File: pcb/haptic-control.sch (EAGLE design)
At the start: 71 parts, among them J1 PAD1X3_5MM-2P, J2 PAD1X3_5MM-2P, M1 SPH0641LM4H-1, U1 CC2642R, U10 FS8205, U2 SST26VF064B, U3 ICM20948, U4 74LVC1G17, U5 MCP1700T-1802TT, U6 PCA9306-DCU, U7 MTCH6301, U8 BQ51050B, U9 FS312F-G, X1 48MHz, X2 32.768kHz

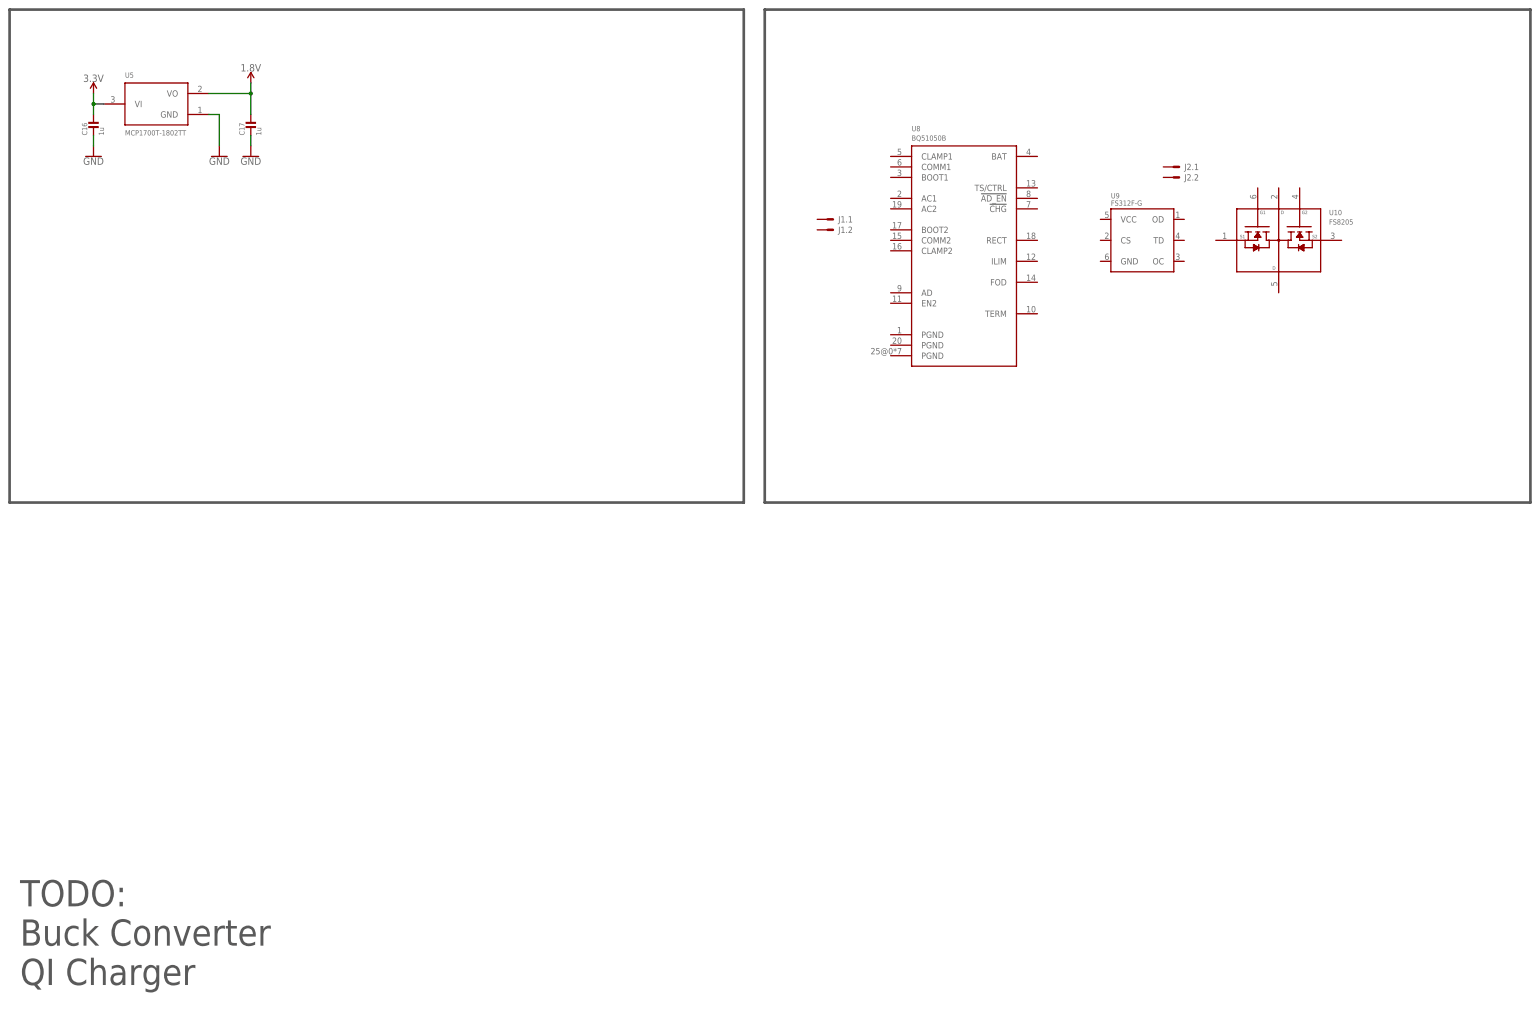
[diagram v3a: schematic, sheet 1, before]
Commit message: added LRA drivers, added FSRs
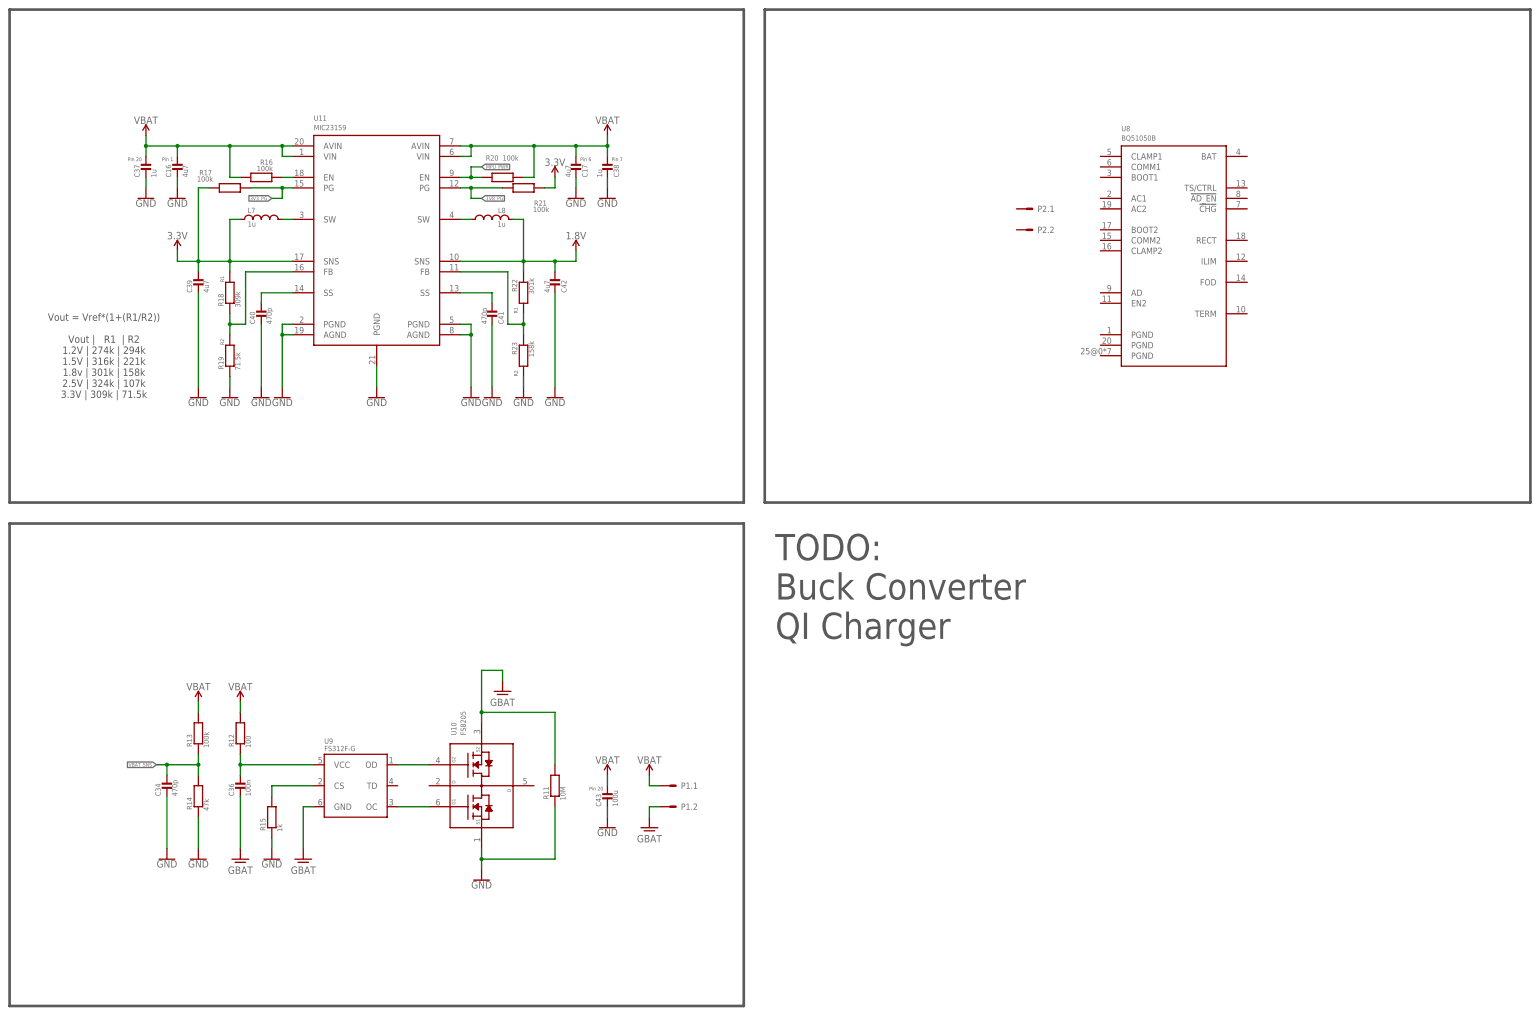
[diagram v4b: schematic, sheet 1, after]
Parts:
- removed J1, J2: PAD1X3_5MM-2P, Connectors > Other:PAD1X3_5MM-2P
- removed TP1, TP2, TP3: TEST_POINT, Utility > Board:TEST_POINT
- added C36, C44, C45: 100n, Passive Components > Capacitors > Multilayer Ceramic Capacitors MLCC:MLCC_0402
- added C37, C38, C46, C47: 1u, Passive Components > Capacitors > Multilayer Ceramic Capacitors MLCC:MLCC0603
- added C39, C42: 4u7, Passive Components > Capacitors > Multilayer Ceramic Capacitors MLCC:MLCC0603
- added C40, C41: 470p, Passive Components > Capacitors > Multilayer Ceramic Capacitors MLCC:MLCC_0402
- added C43: 100u, Passive Components > Capacitors > Multilayer Ceramic Capacitors MLCC:MLCC_1206
- added JP1, JP2: JUMPER-SMT_2_NC_TRACE_SILK, Utility > Board:JUMPER-SMT_2_NC_TRACE_SILK
- added L7, L8: 1u, Passive Components > Inductors, Chokes & Coils:INDUCTOR_NC_0805
- added P1, P2, P3, P4: 2P-PAD_1X3.5, Connectors > Other:2P-PAD_1X3.5
- added R10, R13, R16, R17, R20, R21: 100k, Passive Components > Resistors > Chip Resistors:RESISTOR_0402
- added R11: 10M, Passive Components > Resistors > Chip Resistors:RESISTOR_0402
- added R12: 100, Passive Components > Resistors > Chip Resistors:RESISTOR_0402
- added R14: 47k, Passive Components > Resistors > Chip Resistors:RESISTOR_0402
- added R15: 1k, Passive Components > Resistors > Chip Resistors:RESISTOR_0402
- added R18: 309k, Passive Components > Resistors > Chip Resistors:RESISTOR_0402
- added R19: 71.5k, Passive Components > Resistors > Chip Resistors:RESISTOR_0402
- added R22: 301k, Passive Components > Resistors > Chip Resistors:RESISTOR_0402
- added R23: 158k, Passive Components > Resistors > Chip Resistors:RESISTOR_0402
- added R24, R25, R26, R27: FSR400-SHORT-TAIL, Interlink:FSR400-SHORT-TAIL
- added U11: MIC23159, Microchip:MIC23159
- added U12: DRV2605L, Texas Instruments:DRV2605L
- C16, C17: value 1u -> 4u7
- C27: value 100u -> 22u; device Passive Components > Capacitors > Multilayer Ceramic Capacitors MLCC:MLCC_1206 -> Passive Components > Capacitors > Multilayer Ceramic Capacitors MLCC:MLCC0603
- C33: device Passive Components > Capacitors > Multilayer Ceramic Capacitors MLCC:MLCC_0402 -> Passive Components > Capacitors > Multilayer Ceramic Capacitors MLCC:MLCC_SEL
- C34: value DNP -> 470p
- R8, R9: value 200k -> 4k7
- U5: value MCP1700T-1802TT -> DRV2605L; device Power > LDO Voltage Regulators:MCP1700T-1802TT -> Texas Instruments:DRV2605L
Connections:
- new net 1V8_PG: R21.P$1, U11.PG@1
- new net 3V3_PG: R17.P$1, U11.PG@0
- new net GBAT: C36.P$2, P1.2.S, R11.P$2, U10.S2, U9.GND
- new net LRA_EN: U12.EN, U5.EN
- new net MPU_PWR: R20.P$1, U11.EN@1
- new net N$12: C33.I, L6.P$1
- new net N$13: C32.P$1, C33.O2
- new net N$21: U10.G2, U9.OD
- new net N$22: U10.G1, U9.OC
- new net N$23: C36.P$1, R12.P$1, U9.VCC
- new net N$24: R15.P$2, U9.CS
- new net N$25: R18.P$1, R19.P$2, U11.FB@0
- new net N$26: R16.P$1, U11.EN@0
- new net N$27: P3.1.S, U5.OUT+
- new net N$28: L7.P$2, U11.SW@0
- new net N$29: C40.P$1, U11.SS@0
- new net N$30: L8.P$2, U11.SW@1
- new net N$31: C41.P$1, U11.SS@1
- new net N$32: R22.P$2, R23.P$1, U11.FB@1
- new net N$33: P3.2.S, U5.OUT-
- new net N$34: P4.1.S, U12.OUT+
- new net N$35: P4.2.S, U12.OUT-
- new net N$36: C46.P$1, U5.REG
- new net N$37: C47.P$1, U12.REG
- new net VBAT: C16.P$1, C17.P$1, C37.P$1, C38.P$1, C43.P$1, C44.P$1, C45.P$1, P1.1.S, R12.P$2, R13.P$2, R16.P$2, R20.P$2, U11.AVIN@0, U11.AVIN@1, U11.VIN@0, U11.VIN@1, U12.VDD@0, U12.VDD@1, U5.VDD@0, U5.VDD@1
- new net VBAT_SNS: C34.P$1, R13.P$1, R14.P$2
- net 1.8V: now also C18.P$1, C42.P$1, L8.P$1, R22.P$1, U11.SNS@1, U3.VDD; no longer C17.P$1, U5.VO
- net 3.3V: now also C39.P$1, L7.P$1, R10.P$2, R17.P$2, R18.P$2, R21.P$2, U11.SNS@0; no longer C16.P$1, C18.P$1, U3.VDD, U5.VI
- net DBG_RX: now also JP2.1; no longer TP2.S, U1.DIO_27
- net DBG_TX: now also JP1.1; no longer TP1.S, U1.DIO_28
- net FLASH_CS: no longer U1.DIO_30
- net FLASH_MISO: no longer U1.DIO_18
- net FLASH_MOSI: no longer U1.DIO_19
- net GND: now also C34.P$2, C37.P$2, C38.P$2, C39.P$2, C40.P$2, C41.P$2, C42.P$2, C43.P$2, C44.P$2, C45.P$2, C46.P$2, C47.P$2, R11.P$1, R14.P$1, R15.P$1, R19.P$1, R23.P$2, U10.S1, U11.AGND@0, U11.AGND@1, U11.PGND@0, U11.PGND@1, U11.PGND@2, U12.GND, U12.IN/TRIG, U5.IN/TRIG; no longer TP3.S
- net I2S_CLK: no longer U1.DIO_21
- net I2S_DATIN: no longer U1.DIO_8
- net JTAG_TDI/FLASH_MOSI: no longer U1.DIO_17
- net JTAG_TDO: no longer U1.DIO_16
- net MPU_INT: no longer U1.DIO_3
- net N$18: now also A1.SIGNAL, C33.O1; no longer C32.P$1, C33.P$2
- net N$19: now also JP2.2, TC1-5(GND/5V).S; no longer C33.P$1, C34.P$2, L6.P$1
- net N$20: now also JP1.2, TC1-7(RTCK).S; no longer A1.SIGNAL, C34.P$1
- net SCL: now also U12.SCL, U5.SCL; no longer U1.DIO_1
- net SDA: now also U12.SDA, U5.SDA; no longer U1.DIO_0
- net TC_!RESET: now also R10.P$1
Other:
- note added: "C33 is a 0402 selectable"
- note added: "Pin 1"
- note added: "Pin 20"
- note added: "Pin 6"
- note added: "Pin 7"
- note added: "Pin 8"
- note added: "R1"
- note added: "R2"
- note added: "TODO: Capacitive Buttons Capacitive Matrix FSR conditioning"
- note added: "Vout = Vref*(1+(R1/R2)) Vout | R1 | R2 1.2V | 274k | 294k 1.5V | 316k | 221k 1.8v | 301k | 158k 2.5V | 324k | 107k 3.3V | 309k | 71.5k"
- note removed: "Mount either C33 or C34"
- note removed: "TODO: Capacitive Buttons Capacitive Matrix Haptic Feedback LRA"
- moved on the sheet: C16, C17, C22, C23, C24, C25, C26, C27, M1, R3, R6, TC1-5(GND/5V)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

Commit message: TODO: qi, mcu connect
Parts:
- added C48, C49, C50, C51: 470p, Passive Components > Capacitors > Multilayer Ceramic Capacitors MLCC:MLCC_0402
- added F1: 500mA, PTC Fuses:PTC0805
- added R28, R29, R30, R31: 3.4k, Passive Components > Resistors > Chip Resistors:RESISTOR_0402
- R14: value 47k -> 49.9k
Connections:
- net JTAG_TDI/FLASH_MOSI renamed FLASH_SCK
- new net FSR_CH_N: C49.P$1, R25.2, R29.P$2
- new net FSR_CH_P: C48.P$1, R24.2, R28.P$2
- new net FSR_VOL_N: C51.P$1, R27.2, R30.P$2
- new net FSR_VOL_P: C50.P$1, R26.2, R31.P$2
- new net N$38: F1.1, P1.1.S
- net 3.3V: now also R24.1, R25.1, R26.1, R27.1
- net GND: now also C48.P$2, C49.P$2, C50.P$2, C51.P$2, R28.P$1, R29.P$1, R30.P$1, R31.P$1
- net JTAG_TDI: now also U1.DIO_17
- net JTAG_TDO: now also U1.DIO_16
- net SCL: now also R3.P$1
- net SDA: no longer R3.P$1
- net VBAT: now also F1.2; no longer P1.1.S
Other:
- note added: "ADC Ref: 1.43V"
- note added: "Rfsr = 4.5k @ 1kg"
- note added: "TODO: Capacitive Matrix"
- note added: "TODO: QI Charger"
- note added: "VBAT_SNS = 1.43V @ VBAT = 4.295V"
- note added: "Vout = V * (R1 / R1 + Rfsr)"
- note removed: "TODO: Buck Converter QI Charger"
- note removed: "TODO: Capacitive Buttons Capacitive Matrix FSR conditioning"
- moved on the sheet: C22, C34, C36, C43, C44, C45, C46, C47, M1, P1.1, P1.2, P3.1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

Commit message: Add QI and conect MCU
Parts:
- removed R1: 100k, Passive Components > Resistors > Chip Resistors:RESISTOR_0402
- added C52, C55, C56: 470p, Passive Components > Capacitors > Multilayer Ceramic Capacitors MLCC:MLCC_0402
- added C53, C57, C58, C59, C61: 100n, Passive Components > Capacitors > Multilayer Ceramic Capacitors MLCC:MLCC_0402
- added C54: 1u, Passive Components > Capacitors > Multilayer Ceramic Capacitors MLCC:MLCC0603
- added C60: 10u, Passive Components > Capacitors > Multilayer Ceramic Capacitors MLCC:MLCC0603
- added JP3: JUMPER-SMT_2_NC_TRACE_SILK, Utility > Board:JUMPER-SMT_2_NC_TRACE_SILK
- added R32, R34, R36: 3.4k, Passive Components > Resistors > Chip Resistors:RESISTOR_0402
- added R33, R35: FSR400-SHORT-TAIL, Interlink:FSR400-SHORT-TAIL
- added R37: 100k, Passive Components > Resistors > Chip Resistors:RESISTOR_0402
- C1: value 100n -> 1u; device Passive Components > Capacitors > Multilayer Ceramic Capacitors MLCC:MLCC_0402 -> Passive Components > Capacitors > Multilayer Ceramic Capacitors MLCC:MLCC0603
- C10, C9: value 12p -> 22n
- C11, C12: value DNP -> 470n
- C13: value 1u -> 470p; device Passive Components > Capacitors > Multilayer Ceramic Capacitors MLCC:MLCC0603 -> Passive Components > Capacitors > Multilayer Ceramic Capacitors MLCC:MLCC_0402
- C14, C15, C19, C2: value 100n -> 4u7; device Passive Components > Capacitors > Multilayer Ceramic Capacitors MLCC:MLCC_0402 -> Passive Components > Capacitors > Multilayer Ceramic Capacitors MLCC:MLCC0603
- C16, C39: value 4u7 -> 1u
- C18: value 100n -> 470p
- C21: value 100n -> 100u; device Passive Components > Capacitors > Multilayer Ceramic Capacitors MLCC:MLCC_0402 -> Passive Components > Capacitors > Multilayer Ceramic Capacitors MLCC:MLCC_1206
- C22, C44: value 100n -> DNP
- C23, C36: value 100n -> 22u; device Passive Components > Capacitors > Multilayer Ceramic Capacitors MLCC:MLCC_0402 -> Passive Components > Capacitors > Multilayer Ceramic Capacitors MLCC:MLCC0603
- C24: value 10u -> 1p8; device Passive Components > Capacitors > Multilayer Ceramic Capacitors MLCC:MLCC0603 -> Passive Components > Capacitors > Multilayer Ceramic Capacitors MLCC:MLCC_0402
- C26: value 100n -> 12p; device Passive Components > Capacitors > Multilayer Ceramic Capacitors MLCC:MLCC_0402 -> Passive Components > Capacitors > Multilayer Ceramic Capacitors MLCC:MLCC_SEL
- C27: value 22u -> 100n; device Passive Components > Capacitors > Multilayer Ceramic Capacitors MLCC:MLCC0603 -> Passive Components > Capacitors > Multilayer Ceramic Capacitors MLCC:MLCC_0402
- C28, C29: value 1p -> 100n
- C30: value 12p -> 1p
- C31: value 1p -> 22u; device Passive Components > Capacitors > Multilayer Ceramic Capacitors MLCC:MLCC_0402 -> Passive Components > Capacitors > Multilayer Ceramic Capacitors MLCC:MLCC0603
- C32: value 1p8 -> 100n
- C33: value 12p -> 1p; device Passive Components > Capacitors > Multilayer Ceramic Capacitors MLCC:MLCC_SEL -> Passive Components > Capacitors > Multilayer Ceramic Capacitors MLCC:MLCC_0402
- C34: value 470p -> 1p
- C35: value DNP -> 12p
- C37, C38, C46, C47: value 1u -> 100n; device Passive Components > Capacitors > Multilayer Ceramic Capacitors MLCC:MLCC0603 -> Passive Components > Capacitors > Multilayer Ceramic Capacitors MLCC:MLCC_0402
- C4: value 22u -> 4u7
- C40, C48, C49: value 470p -> 100n
- C41: value 470p -> DNP
- C42: value 4u7 -> 12p; device Passive Components > Capacitors > Multilayer Ceramic Capacitors MLCC:MLCC0603 -> Passive Components > Capacitors > Multilayer Ceramic Capacitors MLCC:MLCC_0402
- C43: value 100u -> 12p; device Passive Components > Capacitors > Multilayer Ceramic Capacitors MLCC:MLCC_1206 -> Passive Components > Capacitors > Multilayer Ceramic Capacitors MLCC:MLCC_0402
- C5: value 100n -> 1n
- C50: value 470p -> 1u; device Passive Components > Capacitors > Multilayer Ceramic Capacitors MLCC:MLCC_0402 -> Passive Components > Capacitors > Multilayer Ceramic Capacitors MLCC:MLCC0603
- C6: value 22u -> 470p; device Passive Components > Capacitors > Multilayer Ceramic Capacitors MLCC:MLCC0603 -> Passive Components > Capacitors > Multilayer Ceramic Capacitors MLCC:MLCC_0402
- C7, C8: value 100n -> 10n
- L1: value 6u8 -> 1u
- L2: value BLM18HE152SN1 -> 1u; device Passive Components > Inductors, Chokes & Coils:INDUCTOR_NC_0603 -> Passive Components > Inductors, Chokes & Coils:INDUCTOR_NC_0805
- L3: value 2n4 -> BLM18HE152SN1; device Passive Components > Inductors, Chokes & Coils:INDUCTOR_NC_0402 -> Passive Components > Inductors, Chokes & Coils:INDUCTOR_NC_0603
- L4: value 2n4 -> 2N
- L6: value 2N -> 2n4
- L7: value 1u -> 2n4; device Passive Components > Inductors, Chokes & Coils:INDUCTOR_NC_0805 -> Passive Components > Inductors, Chokes & Coils:INDUCTOR_NC_0402
- L8: value 1u -> 6u8
- R11: value 10M -> 1k2
- R12: value 100 -> 140
- R14: value 49.9k -> 10k
- R15: value 1k -> 100k
- R16: value 100k -> 49.9k
- R17: value 100k -> 100
- R18: value 309k -> 1k
- R19: value 71.5k -> 10M
- R2: value 100k -> 309k
- R22: value 301k -> 4k7
- R23: value 158k -> 4k7
- R24, R25: value FSR400-SHORT-TAIL -> 100k; device Interlink:FSR400-SHORT-TAIL -> Passive Components > Resistors > Chip Resistors:RESISTOR_0402
- R26, R27: value FSR400-SHORT-TAIL -> 4k7; device Interlink:FSR400-SHORT-TAIL -> Passive Components > Resistors > Chip Resistors:RESISTOR_0402
- R28: value 3.4k -> 200k
- R29, R31: value 3.4k -> FSR400-SHORT-TAIL; device Passive Components > Resistors > Chip Resistors:RESISTOR_0402 -> Interlink:FSR400-SHORT-TAIL
- R3: value 4k7 -> 71.5k
- R6: value 4k7 -> 100k
- R7: value 200k -> 301k
- R8: value 4k7 -> 158k
- R9: value 4k7 -> 2k43
- U1: value CC2642R -> MIC23159; device Texas Instruments:CC2642R -> Microchip:MIC23159
- U10: value FS8205 -> DRV2605L; device Fortune:FS8205 -> Texas Instruments:DRV2605L
- U11: value MIC23159 -> DRV2605L; device Microchip:MIC23159 -> Texas Instruments:DRV2605L
- U12: value DRV2605L -> MTCH6301; device Texas Instruments:DRV2605L -> Microchip:MTCH6301
- U2: value SST26VF064B -> BQ51050B; device Microchip:SST26VF064B -> Texas Instruments:BQ51050B
- U3: value ICM20948 -> FS312F-G; device TDK:ICM20948 -> Fortune:FS312F-G
- U4: value 74LVC1G17 -> FS8205; device Semiconductors > Integrated Circuits - ICs > Logic ICs > Logic Gates:74LVC1G17 -> Fortune:FS8205
- U5: value DRV2605L -> CC2642R; device Texas Instruments:DRV2605L -> Texas Instruments:CC2642R
- U6: value PCA9306-DCU -> SST26VF064B; device Texas Instruments:PCA9306-DCU -> Microchip:SST26VF064B
- U7: value MTCH6301 -> 74LVC1G17; device Microchip:MTCH6301 -> Semiconductors > Integrated Circuits - ICs > Logic ICs > Logic Gates:74LVC1G17
- U8: value BQ51050B -> ICM20948; device Texas Instruments:BQ51050B -> TDK:ICM20948
- U9: value FS312F-G -> PCA9306-DCU; device Fortune:FS312F-G -> Texas Instruments:PCA9306-DCU
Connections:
- removed net 3V3_PG: R17.P$1, U11.PG@0
- new net !QI_CHG: R10.P$1, U2.!CHG, U5.DIO_12
- new net N$39: R11.P$2, R12.P$2, R13.P$1, U2.FOD
- new net N$40: R11.P$1, U2.ILIM
- new net N$41: C17.P$1, R13.P$2, U2.RECT
- new net N$42: R9.P$2, U2.TERM
- new net N$43: C11.P$1, U2.CLAMP1
- new net N$44: C9.P$1, U2.COMM1
- new net N$45: C7.P$1, U2.BOOT1
- new net N$46: C12.P$1, U2.CLAMP2
- new net N$47: C10.P$1, U2.COMM2
- new net N$48: C8.P$1, U2.BOOT2
- new net N$49: C10.P$2, C12.P$2, C5.P$2, C8.P$2, P1.2.S, U2.AC2
- new net N$50: C11.P$2, C3.P$1, C5.P$1, C7.P$2, C9.P$2, U2.AC1
- new net N$51: C3.P$2, P1.1.S
- new net N$53: JP3.2, U1.PG@0
- new net QI_CTRL: R14.P$2, U2.TS/CTRL, U5.DIO_13
- net 1.8V: now also C14.P$1, C46.P$1, C47.P$1, L2.P$1, R26.P$2, R27.P$2, R7.P$1, U1.SNS@1, U8.VDD, U8.VDDIO, U9.VREF1; no longer C18.P$1, C19.P$1, C42.P$1, L8.P$1, R22.P$1, R8.P$2, R9.P$2, U11.SNS@1, U3.VDD, U3.VDDIO, U6.VREF1
- net 1V8_PG: now also R6.P$1, U1.PG@1, U5.DIO_14; no longer R21.P$1, U11.PG@1
- net 3.3V: now also C4.P$1, C40.P$1, C57.P$1, C58.P$1, C59.P$1, C61.P$1, L1.P$1, L3.P$1, R22.P$2, R23.P$2, R24.P$2, R25.P$2, R28.P$2, R29.1, R31.1, R33.1, R35.1, R37.P$2, U1.SNS@0, U12.VDD@0, U12.VDD@1, U12.VDD@2, U6.VCC, U7.PW.GND; no longer C15.P$1, C22.P$1, C25.P$1, C26.P$1, C27.P$1, C39.P$1, L2.P$1, L7.P$1, R17.P$2, R18.P$2, R24.1, R25.1, R26.1, R27.1, R3.P$2, R4.P$2, R5.P$2, R7.P$2, U11.SNS@0, U2.VCC, U4.PW.GND, U7.VDD@0, U7.VDD@1, U7.VDD@2
- net DBG_RX: now also U5.DIO_29
- net DBG_TX: now also U5.DIO_30
- net FLASH_CS: now also R21.P$1, U5.DIO_4, U6.!CS!; no longer R2.P$1, U2.!CS!
- net FLASH_MISO: now also U5.DIO_6, U6.MISO/IO1; no longer U2.MISO/IO1
- net FLASH_MOSI: now also U5.DIO_7, U6.MOSI/IO0; no longer U2.MOSI/IO0
- net FLASH_SCK: now also U5.DIO_5, U6.SCK; no longer U2.SCK
- net FSR_CH_N: now also C52.P$1, R31.2, R32.P$2, U5.DIO_25; no longer C49.P$1, R25.2, R29.P$2
- net FSR_CH_P: now also C51.P$1, R29.2, R30.P$2, U5.DIO_26; no longer C48.P$1, R24.2, R28.P$2
- net FSR_VOL_N: now also C56.P$1, R35.2, R36.P$2, U5.DIO_24; no longer C51.P$1, R27.2, R30.P$2
- net FSR_VOL_P: now also C55.P$1, R33.2, R34.P$2, U5.DIO_27; no longer C50.P$1, R26.2, R31.P$2
- net GBAT: now also C20.P$2, P2.2.S, R19.P$2, U3.GND, U4.S2; no longer C36.P$2, P1.2.S, R11.P$2, U10.S2, U9.GND
- net GND: now also C28.P$2, C29.P$2, C32.P$2, C34.P$1, C36.P$2, C52.P$2, C53.P$2, C54.P$2, C55.P$2, C56.P$2, C57.P$2, C58.P$2, C59.P$2, C60.P$2, C61.P$2, R12.P$1, R16.P$1, R18.P$1, R3.P$1, R32.P$1, R34.P$1, R36.P$1, R8.P$2, R9.P$1, U1.AGND@0, U1.AGND@1, U1.PGND@0, U1.PGND@1, U1.PGND@2, U10.GND, U10.IN/TRIG, U11.GND, U11.IN/TRIG, U12.GND@0, U12.GND@1, U12.GND@2, U12.GND@3, U12.GND@4, U2.AD, U2.PGND@0, U2.PGND@1, U2.PGND@2, U4.S1, U7.PW.VCC, U8.GND, U8.SDO, U9.GND; no longer C10.P$2, C11.P$2, C12.P$2, C20.P$2, C24.P$2, C26.P$2, C28.P$1, C3.P$2, C34.P$2, C5.P$2, C7.P$2, C8.P$2, C9.P$2, R11.P$1, R15.P$1, R23.P$2, R28.P$1, R29.P$1, R31.P$1, U1.GND, U10.S1, U11.AGND@0, U11.AGND@1, U11.PGND@0, U11.PGND@1, U11.PGND@2, U12.GND, U12.IN/TRIG, U2.GND, U3.GND, U3.SDO, U4.PW.VCC, U5.IN/TRIG, U7.GND@0, U7.GND@1, U7.GND@2, U7.GND@3, U7.GND@4
- net I2S_CLK: now also U5.DIO_20
- net I2S_DATIN: now also U5.DIO_19
- net JTAG_TCKC: now also U5.JTAG_TCKC; no longer U1.JTAG_TCKC
- net JTAG_TDI: now also U5.DIO_17; no longer U1.DIO_17
- net JTAG_TDO: now also U5.DIO_16; no longer U1.DIO_16
- net JTAG_TMSC: now also U5.JTAG_TMSC; no longer U1.JTAG_TMSC
- net LRA_EN: now also U10.EN, U11.EN, U5.DIO_1; no longer U12.EN, U5.EN
- net MCU_!RESET: now also C25.P$1, JP3.1, R20.P$1, U5.!RESET; no longer C14.P$1, R1.P$1, U1.!RESET
- net MCU_SW: now also L8.P$1, U5.DCDC_SW; no longer L1.P$1, U1.DCDC_SW
- net MPU_INT: now also U5.DIO_18, U7.1.Y; no longer U4.1.Y
- net MPU_PWR: now also R5.P$1, U1.EN@1, U5.DIO_15; no longer R20.P$1, U11.EN@1
- net N$1: now also C34.P$2, L6.P$2, U5.RF_N; no longer C28.P$2, L4.P$2, U1.RF_N
- net N$10: now also C60.P$1, U12.VCAP; no longer C24.P$1, U7.VCAP
- net N$11: now also C48.P$1, R28.P$1, U9.EN, U9.VREF2; no longer C21.P$1, R7.P$1, U6.EN, U6.VREF2
- net N$12: now also C26.I, L4.P$1; no longer C33.I, L6.P$1
- net N$13: now also C24.P$1, C26.O2; no longer C32.P$1, C33.O2
- net N$14: now also C35.P$1, L7.P$1; no longer C30.P$1, L3.P$1
- net N$15: now also C33.P$1, L6.P$1; no longer C29.P$1, L4.P$1
- net N$16: now also C30.P$1, L4.P$2; no longer C31.P$1, L6.P$2
- net N$17: now also C22.P$1, C24.P$2; no longer C32.P$2, C35.P$1
- net N$18: now also C26.O1; no longer C33.O1
- net N$2: now also C39.P$1, U5.DCOUPL; no longer C13.P$1, U1.DCOUPL
- net N$21: now also U3.OD, U4.G2; no longer U10.G2, U9.OD
- net N$22: now also U3.OC, U4.G1; no longer U10.G1, U9.OC
- net N$23: now also C20.P$1, R17.P$1, U3.VCC; no longer C36.P$1, R12.P$1, U9.VCC
- net N$24: now also R18.P$2, U3.CS; no longer R15.P$2, U9.CS
- net N$25: now also R2.P$1, R3.P$2, U1.FB@0; no longer R18.P$1, R19.P$2, U11.FB@0
- net N$26: now also R4.P$1, U1.EN@0; no longer R16.P$1, U11.EN@0
- net N$27: now also U10.OUT+; no longer U5.OUT+
- net N$28: now also L1.P$2, U1.SW@0; no longer L7.P$2, U11.SW@0
- net N$29: now also C6.P$1, U1.SS@0; no longer C40.P$1, U11.SS@0
- net N$3: now also C33.P$2, L7.P$2, U5.RF_P; no longer C29.P$2, L3.P$2, U1.RF_P
- net N$30: now also L2.P$2, U1.SW@1; no longer L8.P$2, U11.SW@1
- net N$31: now also C13.P$1, U1.SS@1; no longer C41.P$1, U11.SS@1
- net N$32: now also R7.P$2, R8.P$1, U1.FB@1; no longer R22.P$2, R23.P$1, U11.FB@1
- net N$33: now also U10.OUT-; no longer U5.OUT-
- net N$34: now also U11.OUT+; no longer U12.OUT+
- net N$35: now also U11.OUT-; no longer U12.OUT-
- net N$36: now also C50.P$1, U10.REG; no longer C46.P$1, U5.REG
- net N$37: now also C54.P$1, U11.REG; no longer C47.P$1, U12.REG
- net N$38: now also P2.1.S; no longer P1.1.S
- net N$4: now also U7.1.A, U8.INT; no longer U3.INT, U4.1.A
- net N$5: now also R26.P$1, U8.SCL, U9.SCL1; no longer R8.P$1, U3.SCL, U6.SCL1
- net N$6: now also R27.P$1, U8.SDI, U9.SDA1; no longer R9.P$1, U3.SDI, U6.SDA1
- net N$7: now also R24.P$1, U6.!WP!/IO2; no longer R4.P$1, U2.!WP!/IO2
- net N$8: now also R25.P$1, U6.!HOLD!/IO3; no longer R5.P$1, U2.!HOLD!/IO3
- net N$9: now also C45.P$1, U8.REGOUT; no longer C20.P$1, U3.REGOUT
- net PCAP_RX0: now also U12.RX0; no longer U7.RX0
- net PCAP_RX1: now also U12.RX1; no longer U7.RX1
- net PCAP_RX10: now also U12.RX10; no longer U7.RX10
- net PCAP_RX11: now also U12.RX11; no longer U7.RX11
- net PCAP_RX12: now also U12.RX12; no longer U7.RX12
- net PCAP_RX2: now also U12.RX2; no longer U7.RX2
- net PCAP_RX3: now also U12.RX3; no longer U7.RX3
- net PCAP_RX4: now also U12.RX4; no longer U7.RX4
- net PCAP_RX5: now also U12.RX5; no longer U7.RX5
- net PCAP_RX6: now also U12.RX6; no longer U7.RX6
- net PCAP_RX7: now also U12.RX7; no longer U7.RX7
- net PCAP_RX8: now also U12.RX8; no longer U7.RX8
- net PCAP_RX9: now also U12.RX9; no longer U7.RX9
- net PCAP_TX0: now also U12.TX0; no longer U7.TX0
- net PCAP_TX1: now also U12.TX1; no longer U7.TX1
- net PCAP_TX10: now also U12.TX10; no longer U7.TX10
- net PCAP_TX11: now also U12.TX11; no longer U7.TX11
- net PCAP_TX12: now also U12.TX12; no longer U7.TX12
- net PCAP_TX13: now also U12.TX13; no longer U7.TX13
- net PCAP_TX14: now also U12.TX14; no longer U7.TX14
- net PCAP_TX15: now also U12.TX15; no longer U7.TX15
- net PCAP_TX16: now also U12.TX16; no longer U7.TX16
- net PCAP_TX17: now also U12.TX17; no longer U7.TX17
- net PCAP_TX2: now also U12.TX2; no longer U7.TX2
- net PCAP_TX3: now also U12.TX3; no longer U7.TX3
- net PCAP_TX4: now also U12.TX4; no longer U7.TX4
- net PCAP_TX5: now also U12.TX5; no longer U7.TX5
- net PCAP_TX6: now also U12.TX6; no longer U7.TX6
- net PCAP_TX7: now also U12.TX7; no longer U7.TX7
- net PCAP_TX8: now also U12.TX8; no longer U7.TX8
- net PCAP_TX9: now also U12.TX9; no longer U7.TX9
- net SCL: now also R22.P$1, R23.P$1, U10.SCL, U11.SCL, U5.DIO_9, U9.SCL2; no longer R3.P$1, R6.P$1, U5.SCL, U6.SCL2, U7.SCL
- net SDA: now also U10.SDA, U11.SDA, U5.DIO_10, U9.SDA2; no longer U5.SDA, U6.SDA2, U7.SDA
- net TC_!RESET: now also R37.P$1, U12.!RESET, U5.DIO_21; no longer R10.P$1, U7.!RESET
- net TC_INT: now also U12.INT, U5.DIO_22; no longer U7.INT
- net VBAT: now also C1.P$1, C15.P$1, C19.P$1, C2.P$1, C21.P$1, C49.P$1, C53.P$1, R15.P$2, R17.P$2, R4.P$2, R5.P$2, U1.AVIN@0, U1.AVIN@1, U1.VIN@0, U1.VIN@1, U10.VDD@0, U10.VDD@1, U11.VDD@0, U11.VDD@1, U2.BAT; no longer C17.P$1, C37.P$1, C38.P$1, C43.P$1, C44.P$1, C45.P$1, R12.P$2, R13.P$2, R16.P$2, R20.P$2, U11.AVIN@0, U11.AVIN@1, U11.VIN@0, U11.VIN@1, U12.VDD@0, U12.VDD@1, U5.VDD@0, U5.VDD@1
- net VBAT_SNS: now also C18.P$1, R15.P$1, R16.P$2, U5.DIO_23; no longer C34.P$1, R13.P$1, R14.P$2
- net VDDR: now also C36.P$1, C37.P$1, C38.P$1, L8.P$2, U5.VDDR, U5.VDDR_RF; no longer C6.P$1, C7.P$1, C8.P$1, L1.P$2, U1.VDDR, U1.VDDR_RF
- net VDDS: now also C27.P$1, C28.P$1, C29.P$1, C31.P$1, C32.P$1, L3.P$2, R20.P$2, U5.VDDS@0, U5.VDDS@1, U5.VDDS@2, U5.VDDS_DCDC; no longer C1.P$1, C2.P$1, C3.P$1, C4.P$1, C5.P$1, L2.P$2, R1.P$2, U1.VDDS@0, U1.VDDS@1, U1.VDDS@2, U1.VDDS_DCDC
- net XTAL_32K_Q1: now also C43.P$1, U5.X32K_Q1; no longer C10.P$1, U1.X32K_Q1
- net XTAL_32K_Q2: now also C42.P$1, U5.X32K_Q2; no longer C9.P$1, U1.X32K_Q2
- net XTAL_48M_N: now also C44.P$1, U5.X48M_N; no longer C12.P$1, U1.X48M_N
- net XTAL_48M_P: now also C41.P$1, U5.X48M_P; no longer C11.P$1, U1.X48M_P
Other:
- note added: "Icharge = KIlim / RIlim RIlim = R11 + R12 KIlim = 314"
- note removed: "TODO: QI Charger"
